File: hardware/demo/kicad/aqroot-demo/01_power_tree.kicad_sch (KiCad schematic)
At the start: 138 parts, among them J3 USB_C_Receptacle_USB2.0_16P, J4 BATTERY PIGTAIL 26AWG, Q2 NTMD4820N, Q3 NTMD4820N, Q4 BSS138, Q5 AO3401A, Q6 BSS138, Q7 BSS138, Q8 BSS138, Q9 BSS138, SW9 SW_SPDT, U10 USBLC6-2SC6, U11 BQ25185, U12 TPS63020, U13 TPS61023, U14 MAX17048, U18 LTC4368-1, U19 TLV7032, U20 TPS22950-Q1, U21 TPS61023, U22 TPS22950-Q1

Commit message: demo: D-790 close Round-9 — four numbers read at the wrong condition, an image no test had ever compiled, and a pass pair that was never guaranteed to be on
Round-9 external review REJECTED D-789.  Fable passed the design for CAM/order
closure but kept Q2/Q3 open and found two host-test escapes; Astra blocked the
order with 12 findings (0 critical, 3 high, 8 medium, 1 low) plus a procurement
item, and established no unconditional PCB respin.  All of D789-A01..A11 and
S01 are closed here, plus every Fable-specific residual, plus one more this
closeout found itself (R9-N01).

THE THEME IS A NUMBER READ AT THE WRONG CONDITION — a datasheet row the design
does not sit at, a reference frame the product is not in, a network the copper
does not form, and a subtotal inherited from a board that no longer exists.

A11  the display budget line was an INHERITED SUBTOTAL smaller than the
     backlight alone.  181 mA, cited to a 2023 subtotal.  The backlight
     converter's input is now SOLVED from published maxima only and bounded by
     the worst of a CCM treatment, a DCM treatment and TI's own "up to 90 %"
     headline: 211.58 mA at an implied 83.1 %.  The panel's logic side becomes
     a separate LABELLED DECLARED 50 mA allowance, because ILI Technology
     publishes no active-mode supply current at all.  Internal +3V3 1.0632 ->
     1.1438 A.  New first-article C-DISP-01.
A03  a shared impedance was inside both branches and then paralleled.  The
     U12->U20 plane is the MAIN +3V3 plane and now carries I_INTERNAL + the
     accessory budget = 1.5438 A, charged ONCE, outside the per-contact
     branches.  Published Community-Port minimum 2.849642 -> 2.813742 V
     (published >= 2.81 V); fully mated 2.982890 -> 2.918599 V.  No current
     capability reduced.
A02  a JEDEC thetaJA is not a product bound, and the peak envelope is not a
     thermal envelope.  TJ = TA + R_SYS x P_internal + thetaJA x P_U11, with
     R_SYS the enclosure's declared 3.2493 K/W and P_intern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
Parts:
- C29, C30, C31, C32: value 22uF 10V X7R -> 22uF 16V X7R
- Q2: value NTMD4820N -> AO4800; symbol AQROOT_Beta:NTMD4820N -> AQROOT_Beta:AO4800; LCSC C905372 -> C17098; MPN NTMD4820NR2G -> AO4800; Manufacturer onsemi -> Alpha & Omega Semiconductor; Note P2 stage 1 - back-to-back pair, independent failure domain -> D-790 / D789-A01. onsemi NTMD4820NR2G -> Alpha & Omega AO48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; Note2 SOURCING 2026-08-23 (FBV2-S2-002) (B-71) - FIRST-BUILD BLOC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 -> SOURCING, RESTATED AT D-790 / D789-A01. The locked part on 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
- Q3: value NTMD4820N -> AO4800; symbol AQROOT_Beta:NTMD4820N -> AQROOT_Beta:AO4800; LCSC C905372 -> C17098; MPN NTMD4820NR2G -> AO4800; Manufacturer onsemi -> Alpha & Omega Semiconductor; Note P2 stage 2 - SECOND PACKAGE, second failure domain -> D-790 / D789-A01. onsemi NTMD4820NR2G -> Alpha & Omega AO48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; Note2 SOURCING 2026-08-23 (FBV2-S2-002) (B-71) - FIRST-BUILD BLOC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 -> SOURCING, RESTATED AT D-790 / D789-A01. The locked part on 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
- Q4, Q6, Q7, Q8, Q9: Manufacturer onsemi -> Alpha & Omega Semiconductor
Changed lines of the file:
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@@
 			)
 		)
-		(property "Value" "22uF 10V X7R"
+		(property "Value" "22uF 16V X7R"
 			(at 223.52 25.3999 0)
 			(show_name no)
@@
 			)
 		)
-		(property "Value" "22uF 10V X7R"
+		(property "Value" "22uF 16V X7R"
 			(at 266.7 25.3999 0)
 			(show_name no)
@@
 			)
 		)
-		(property "Value" "22uF 10V X7R"
+		(property "Value" "22uF 16V X7R"
 			(at 245.11 25.3999 0)
 			(show_name no)
@@
 			)
 		)
-		(property "Value" "22uF 10V X7R"
+		(property "Value" "22uF 16V X7R"
 			(at 201.93 25.3999 0)
 			(show_name no)
@@
 	)
 	(symbol
-		(lib_id "AQROOT_Beta:NTMD4820N")
+		(lib_id "AQROOT_Beta:AO4800")
 		(at 59.69 299.72 0)
 		(unit 1)
@@
 			)
 		)
-		(property "Value" "NTMD4820N"
+		(property "Value" "AO4800"
 			(at 61.69 296.62 0)
 			(show_name no)
@@
 			)
 		)
-		(property "Note2" "SOURCING 2026-08-23 (FBV2-S2-002) (B-71) - FIRST-BUILD BLOCKER. onsemi NTMD4820NR2G is LCSC C905372 with STOCK 0. A VBsemi clone (C7525084) exists - DO NOT USE IT: these are the back-to-back pass FETs of the LTC4368 reverse-polarity path and the CTO ruling forbids silent substitution of power-path parts. Consign the onsemi part. LCSC/JLC library state verified live on 2026-08-23 through the JLCPCB parts API (D-096). Stock is a snapshot, not a guarantee."
+		(property "Note2" "SOURCING, RESTATED AT D-790 / D789-A01. The locked part on this land is Alpha & Omega Semiconductor AO4800, LCSC C17098, genuine-manufacturer line, stock 5347 on the 2026-09-21 live JLCPCB record (D-096). SUPERSEDED: the onsemi NTMD4820NR2G that used to sit here is RETIRED from this design. The 2026-08-23 FBV2-S2-002 / B-71 note recorded it as a FIRST-BUILD BLOCKER because LCSC C905372 read STOCK 0; D-790 retires it for an ELECTRICAL reason that stands whatever its stock does - it publishes no RDS(on) row below VGS = 4.5 V and a VGS(th) MAXIMUM of 3.0 V, and the LTC4368 guarantees only 3.0 V of gate drive at its lowest published row, so after the three channel drops and R75 between Q2 s source and the LTC4368 s VOUT a worst-corner part was never guaranteed to conduct at all. NO CLONE OR RE-MARKED SUBSTITUTION: these are the back-to-back pass FETs of the LTC4368 reverse-polarity path and the CTO ruling forbids silent substitution of power-path parts. The VBsemi, HXY, UMW, JSMSEMI, MSKSEMI and TECH PUBLIC AO4800-marked lines in the same catalogue are NOT this part and are refused. Buy the AOS line, or an authorised-distributor allocation of it. Stock is a snapshot, not a guarantee."
 			(at 61.69 292.12 0)
 			(hide yes)
@@
 			)
 		)
-		(property "LCSC" "C905372"
+		(property "LCSC" "C17098"
 			(at 61.69 292.12 0)
 			(hide yes)
@@
 			)
 		)
-		(property "Manufacturer" "onsemi"
+		(property "Manufacturer" "Alpha & Omega Semiconductor"
 			(at 61.69 290.62 0)
 			(hide yes)
@@
 			)
 		)
-		(property "MPN" "NTMD4820NR2G"
+		(property "MPN" "AO4800"
 			(at 61.69 289.12 0)
 			(hide yes)
@@
 			)
 		)
-		(property "Note" "P2 stage 1 - back-to-back pair, independent failure domain"
+		(property "Note" "D-790 / D789-A01.  onsemi NTMD4820NR2G -> Alpha & Omega AO4800, SAME SOIC-8 land and SAME pin function map (1,3 = the two sources, 2,4 = the two gates, 5,6 and 7,8 = the two separate drains), so no copper moves.  WHY: the LTC4368 guarantees only dVGATE >= 3.0 V of gate drive at its lowest published row (VIN = 2.5 V, ADI Rev C), this board's BAT_RAW lives between that row and the 5 V one, and after the three channel drops and R75 that stand between Q2's common source and the LTC4368's VOUT the worst-case VGS is about 2.6 V.  The NTMD4820N's VGS(th) MAXIMUM is 3.0 V, so a worst-corner part was NEVER GUARANTEED TO BE ENHANCED AT ALL -- it would pass 250 uA where this path needs amps -- and its lowest published conduction row is VGS = 4.5 V, which this circuit cannot reach.  The AO4800 publishes VGS(th) 0.7/1.1/1.5 V MAX and an RDS(on) MAX of 50 mOhm AT VGS = 2.5 V (AOS Rev 6.1, archived vendor/AOS/aos-ao4800-rev6p1-2023-08.pdf), so both the enhancement and the conduction are GUARANTEED NUMBERS at the gate drive this circuit actually has.  The whole four-channel + R75 + upstream model is solved self-consistently in checks/demo_feature_contract.py F10.  WHAT IT COSTS, STATED: the pass pair is more resistive than the NTMD4820N's unguaranteed 4.5 V row, so it drops more and runs hotter, and D789-A02's enclosure-aware thermal envelope carries that cost explicitly. VGS abs max is +/-12 V against the LTC4368's 10.8 V maximum at its VIN = 5 V row, which is the row AT OR ABOVE this board's BAT_RAW maximum.  VDS 30 V, ID 6.9 A at 25 C.  P2 stage - back-to-back pair, independent failure domain."
 			(at 61.69 287.62 0)
 			(hide yes)
@@
 	)
 	(symbol
-		(lib_id "AQROOT_Beta:NTMD4820N")
+		(lib_id "AQROOT_Beta:AO4800")
 		(at 129.54 299.72 0)
 		(unit 1)
@@
 			)
 		)
-		(property "Value" "NTMD4820N"
+		(property "Value" "AO4800"
 			(at 131.54 296.62 0)
 			(show_name no)
@@
 			)
 		)
-		(property "Note2" "SOURCING 2026-08-23 (FBV2-S2-002) (B-71) - FIRST-BUILD BLOCKER. onsemi NTMD4820NR2G is LCSC C905372 with STOCK 0. A VBsemi clone (C7525084) exists - DO NOT USE IT: these are the back-to-back pass FETs of the LTC4368 reverse-polarity path and the CTO ruling forbids silent substitution of power-path parts. Consign the onsemi part. LCSC/JLC library state verified live on 2026-08-23 through the JLCPCB parts API (D-096). Stock is a snapshot, not a guarantee."
+		(property "Note2" "SOURCING, RESTATED AT D-790 / D789-A01. The locked part on this land is Alpha & Omega Semiconductor AO4800, LCSC C17098, genuine-manufacturer line, stock 5347 on the 2026-09-21 live JLCPCB record (D-096). SUPERSEDED: the onsemi NTMD4820NR2G that used to sit here is RETIRED from this design. The 2026-08-23 FBV2-S2-002 / B-71 note recorded it as a FIRST-BUILD BLOCKER because LCSC C905372 read STOCK 0; D-790 retires it for an ELECTRICAL reason that stands whatever its stock does - it publishes no RDS(on) row below VGS = 4.5 V and a VGS(th) MAXIMUM of 3.0 V, and the LTC4368 guarantees only 3.0 V of gate drive at its lowest published row, so after the three channel drops and R75 between Q2 s source and the LTC4368 s VOUT a worst-corner part was never guaranteed to conduct at all. NO CLONE OR RE-MARKED SUBSTITUTION: these are the back-to-back pass FETs of the LTC4368 reverse-polarity path and the CTO ruling forbids silent substitution of power-path parts. The VBsemi, HXY, UMW, JSMSEMI, MSKSEMI and TECH PUBLIC AO4800-marked lines in the same catalogue are NOT this part and are refused. Buy the AOS line, or an authorised-distributor allocation of it. Stock is a snapshot, not a guarantee."
 			(at 131.54 292.12 0)
 			(hide yes)
@@
 			)
 		)
-		(property "LCSC" "C905372"
+		(property "LCSC" "C17098"
 			(at 131.54 292.12 0)
 			(hide yes)
@@
 			)
 		)
-		(property "Manufacturer" "onsemi"
+		(property "Manufacturer" "Alpha & Omega Semiconductor"
 			(at 131.54 290.62 0)
 			(hide yes)
@@
 			)
 		)
-		(property "MPN" "NTMD4820NR2G"
+		(property "MPN" "AO4800"
 			(at 131.54 289.12 0)
 			(hide yes)
@@
 			)
 		)
-		(property "Note" "P2 stage 2 - SECOND PACKAGE, second failure domain"
+		(property "Note" "D-790 / D789-A01.  onsemi NTMD4820NR2G -> Alpha & Omega AO4800, SAME SOIC-8 land and SAME pin function map (1,3 = the two sources, 2,4 = the two gates, 5,6 and 7,8 = the two separate drains), so no copper moves.  WHY: the LTC4368 guarantees only dVGATE >= 3.0 V of gate drive at its lowest published row (VIN = 2.5 V, ADI Rev C), this board's BAT_RAW lives between that row and the 5 V one, and after the three channel drops and R75 that stand between Q2's common source and the LTC4368's VOUT the worst-case VGS is about 2.6 V.  The NTMD4820N's VGS(th) MAXIMUM is 3.0 V, so a worst-corner part was NEVER GUARANTEED TO BE ENHANCED AT ALL -- it would pass 250 uA where this path needs amps -- and its lowest published conduction row is VGS = 4.5 V, which this circuit cannot reach.  The AO4800 publishes VGS(th) 0.7/1.1/1.5 V MAX and an RDS(on) MAX of 50 mOhm AT VGS = 2.5 V (AOS Rev 6.1, archived vendor/AOS/aos-ao4800-rev6p1-2023-08.pdf), so both the enhancement and the conduction are GUARANTEED NUMBERS at the gate drive this circuit actually has.  The whole four-channel + R75 + upstream model is solved self-consistently in checks/demo_feature_contract.py F10.  WHAT IT COSTS, STATED: the pass pair is more resistive than the NTMD4820N's unguaranteed 4.5 V row, so it drops more and runs hotter, and D789-A02's enclosure-aware thermal envelope carries that cost explicitly. VGS abs max is +/-12 V against the LTC4368's 10.8 V maximum at its VIN = 5 V row, which is the row AT OR ABOVE this board's BAT_RAW maximum.  VDS 30 V, ID 6.9 A at 25 C.  P2 stage - back-to-back pair, independent failure domain."
 			(at 131.54 287.62 0)
 			(hide yes)
@@
 			)
 		)
-		(property "Manufacturer" "onsemi"
+		(property "Manufacturer" "Alpha & Omega Semiconductor"
 			(at 0 0 0)
 			(hide yes)
@@
 			)
 		)
-		(property "Manufacturer" "onsemi"
+		(property "Manufacturer" "Alpha & Omega Semiconductor"
 			(at 0 0 0)
 			(hide yes)
@@
 			)
 		)
-		(property "Manufacturer" "onsemi"
+		(property "Manufacturer" "Alpha & Omega Semiconductor"
 			(at 0 0 0)
 			(hide yes)
@@
 			)
 		)
-		(property "Manufacturer" "onsemi"
+		(property "Manufacturer" "Alpha & Omega Semiconductor"
 			(at 0 0 0)
 			(hide yes)
@@
 			)
 		)
-		(property "Manufacturer" "onsemi"
+		(property "Manufacturer" "Alpha & Omega Semiconductor"
 			(at 0 0 0)
 			(hide yes)

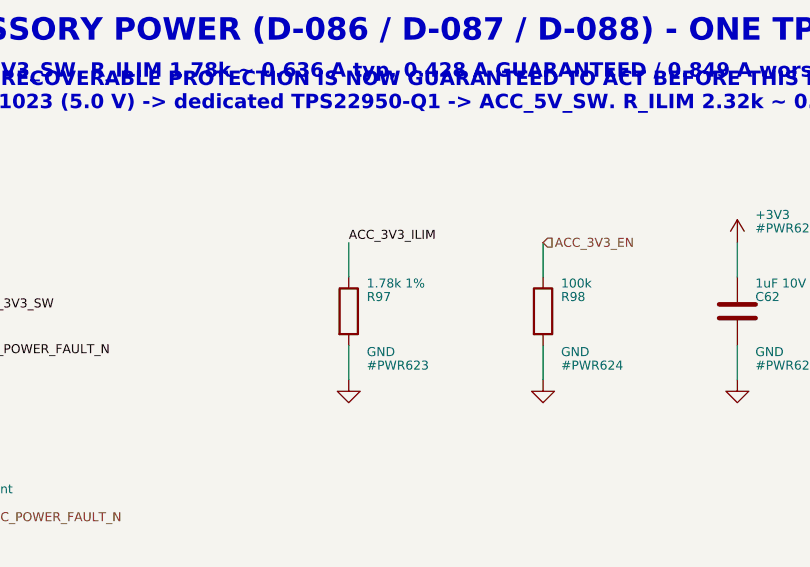
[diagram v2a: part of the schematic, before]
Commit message: demo: D-791 close Round-10 — a floor the node could never reach, a loss model that was only a conduction model, and a gate that was holding a stale procedure in place
Round-10 external review REJECTED D-790.  Fable passed the design for CAM/order
closure with 3 medium / 16 low plus residuals; Astra BLOCKED the order with 15
findings (0 critical, 4 high, 8 medium, 3 low) plus a procurement item, and
established no unconditional PCB respin.

All of D790-A01..A14 and S01 are closed here, plus every Fable complementary
item (F-N01..F-N04, F-V04, F-V05, F-C01, F-C03), plus five this closeout found
itself: R10-N01, R10-N02, R10-N03, and at the verification pass R10-N04 and
R10-N05.

THE THEME IS A NUMBER THAT IS RIGHT ABOUT A STATE THE BOARD CANNOT OCCUPY.

* A03: the firmware's VCELL floors were node voltages BAT_PROTECTED_P cannot
  reach -- 3.85 V there needs >4.3 V upstream and the charger's regulation
  maximum on the pack is 4.221 V -- so the accessory rails this product
  publishes would have been authorised and shed again 400 ms later, on a full
  pack.  New F12 solves the complete cell-to-load network as one fixed point
  and DERIVES three floors: retention 3.20 V, first-rail enable 3.55 V,
  second-rail enable 3.65 V.  Attainability is a clause.
* A02: one electrical network for every sustained mode, states named in
  OBSERVABLE modes, NFC/microSD/IR returned as bounded-duty allowances, TREG
  split into the half it regulates and the half it cannot, and a derived
  30.0 C charge-ambient ceiling.
* A01: the AO4800 conduction row is a ceiling and is now printed, with a 2x
  sensitivity on the declared hot ratio; AO4806 re-examined and re-rejected on
  stock, for the right reason.
* A04: the backlight model gains the four loss terms it was missing,
  211.58 -> 233.13 mA.
* A12 + A10 + A11: the ILIM bound returns to the widest published ratio
  (R97 1.78 -> 1.87 kOhm so U12 stays inside its 2 A rating), BQ OCP and
  TPS22950 RON are read at their own conditions.
* A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
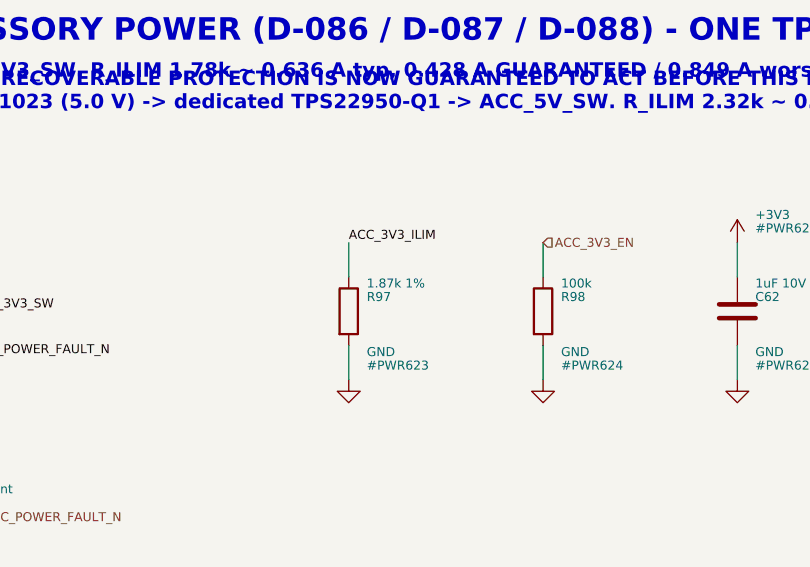
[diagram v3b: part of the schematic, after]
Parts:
- Q4, Q6, Q7, Q8, Q9: Manufacturer Alpha & Omega Semiconductor -> onsemi
- Q5: Manufacturer Alpha & Omega -> Alpha & Omega Semiconductor
- R97: value 1.78k 1% -> 1.87k 1%; LCSC C22849 -> C22850; MPN 0603WAF1781T5E -> 0603WAF1871T5E
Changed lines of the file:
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@@
 			)
 		)
-		(property "Manufacturer" "Alpha & Omega Semiconductor"
+		(property "Manufacturer" "onsemi"
 			(at 0 0 0)
 			(hide yes)
@@
 			)
 		)
-		(property "Manufacturer" "Alpha & Omega"
+		(property "Manufacturer" "Alpha & Omega Semiconductor"
 			(at 242.03 375.71 0)
 			(hide yes)
@@
 			)
 		)
-		(property "Manufacturer" "Alpha & Omega Semiconductor"
+		(property "Manufacturer" "onsemi"
 			(at 0 0 0)
 			(hide yes)
@@
 			)
 		)
-		(property "Manufacturer" "Alpha & Omega Semiconductor"
+		(property "Manufacturer" "onsemi"
 			(at 0 0 0)
 			(hide yes)
@@
 			)
 		)
-		(property "Manufacturer" "Alpha & Omega Semiconductor"
+		(property "Manufacturer" "onsemi"
 			(at 0 0 0)
 			(hide yes)
@@
 			)
 		)
-		(property "Manufacturer" "Alpha & Omega Semiconductor"
+		(property "Manufacturer" "onsemi"
 			(at 0 0 0)
 			(hide yes)
@@
 			)
 		)
-		(property "Value" "1.78k 1%"
+		(property "Value" "1.87k 1%"
 			(at 422.37 258.52 0)
 			(show_name no)
@@
 			)
 		)
-		(property "MPN" "0603WAF1781T5E"
+		(property "MPN" "0603WAF1871T5E"
 			(at 422.37 255.52 0)
 			(hide yes)
@@
 			)
 		)
-		(property "LCSC" "C22849"
+		(property "LCSC" "C22850"
 			(at 422.37 255.52 0)
 			(hide yes)
